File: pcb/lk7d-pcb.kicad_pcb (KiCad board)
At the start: 2 copper layers, 57.2 x 57.2 mm, 32 parts, among them J1 PINHD_1x4_Male, J2 PINHD_1x4_Male, M1 JLCPCB_2DBarcode_5x5mm, SW1 RotaryEncoder_Switch_MP, SW2 RotaryEncoder_Switch_MP, SW3 SW_Push, SW4 SW_Push, SW5 SW_Push, SW6 SW_Push, SW7 SW_Push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

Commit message: Update silkscreen
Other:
- board text added: "C1 and C2 are shared between encoders, solder both for proper filtering."
- board text added: "Documentation: lambdakb.dev/devices/lk7d/"
- board text added: "Only solder one encoder as both of them are wired to the same pins on the MCU."
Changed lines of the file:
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@@
+		(layer "B.SilkS")
+	)
+	(gr_poly
+		(pts
+			(xy 78.675417 39.784027) (xy 78.631132 39.786197) (xy 78.587707 39.789814) (xy 78.545141 39.794878)
+			(xy 78.503433 39.801388) (xy 78.462585 39.809345) (xy 78.422596 39.818749) (xy 78.383465 39.8296)
+			(xy 78.345194 39.841897) (xy 78.307782 39.855642) (xy 78.271228 39.870833) (xy 78.235534 39.88747)
+			(xy 78.200699 39.905555) (xy 78.166722 39.925086) (xy 78.133605 39.946064) (xy 78.101347 39.968489)
+			(xy 78.069552 39.99253) (xy 78.038548 40.018357) (xy 78.008336 40.04597) (xy 77.978914 40.075368)
+			(xy 77.950284 40.106553) (xy 77.922445 40.139523) (xy 77.895398 40.174279) (xy 77.869142 40.210821)
+			(xy 77.843676 40.249149) (xy 77.819002 40.289263) (xy 77.79512 40.331162) (xy 77.772028 40.374848)
+			(xy 77.749728 40.420319) (xy 77.728219 40.467576) (xy 77.707501 40.516619) (xy 77.687574 40.567448)
+			(xy 76.663268 43.255528) (xy 76.648281 43.293664) (xy 76.632976 43.329946) (xy 76.617356 43.364374)
+			(xy 76.601418 43.396949) (xy 76.585165 43.42767) (xy 76.568595 43.456538) (xy 76.551708 43.483551)
+			(xy 76.534505 43.508711) (xy 76.516986 43.532018) (xy 76.49915 43.55347) (xy 76.480997 43.573069)
+			(xy 76.462529 43.590815) (xy 76.443744 43.606707) (xy 76.424642 43.620745) (xy 76.405224 43.632929)
+			(xy 76.38549 43.64326) (xy 76.365314 43.652178) (xy 76.344573 43.660124) (xy 76.323267 43.667098)
+			(xy 76.301396 43.673099) (xy 76.27896 43.678129) (xy 76.255959 43.682187) (xy 76.232393 43.685273)
+			(xy 76.208261 43.687386) (xy 76.183564 43.688528) (xy 76.158303 43.688697) (xy 76.132476 43.687895)
+			(xy 76.106084 43.68612) (xy 76.079127 43.683374) (xy 76.051604 43.679655) (xy 76.023517 43.674964)
+			(xy 75.994864 43.669301) (xy 75.92542 43.651941) (xy 75.769169 44.164093) (xy 75.785988 44.170559)
+			(xy 75.804614 44.176934) (xy 75.82505 44.183218) (xy 75.847294 44.189412) (xy 75.871346 44.195515)
+			(xy 75.897207 44.201528) (xy 75.924877 44.207451) (xy 75.954355 44.213283) (xy 75.985054 44.218709)
+			(xy 76.016385 44.223411) (xy 76.04835 44.22739) (xy 76.080947 44.230645) (xy 76.114177 44.233177)
+			(xy 76.14804 44.234985) (xy 76.182537 44.23607) (xy 76.217666 44.236432) (xy 76.261408 44.235709)
+			(xy 76.304381 44.233538) (xy 76.346585 44.229922) (xy 76.388022 44.224858) (xy 76.428689 44.218347)
+			(xy 76.468588 44.21039) (xy 76.507719 44.200986) (xy 76.54608 44.190136) (xy 76.583674 44.177838)
+			(xy 76.620499 44.164094) (xy 76.656555 44.148903) (xy 76.691842 44.132265) (xy 76.726361 44.114181)
+			(xy 76.760112 44.094649) (xy 76.793093 44.073671) (xy 76.825306 44.051246) (xy 76.856378 44.027194)
+			(xy 76.886658 44.001333) (xy 76.916147 43.973664) (xy 76.944844 43.944186) (xy 76.972751 43.9129)
+			(xy 76.999866 43.879805) (xy 77.02619 43.844902) (xy 77.051723 43.808191) (xy 77.076465 43.769671)
+			(xy 77.100416 43.729342) (xy 77.123575 43.687205) (xy 77.145943 43.64326) (xy 77.16752 43.597506)
+			(xy 77.188306 43.549944) (xy 77.208301 43.500573) (xy 77.227504 43.449394) (xy 77.641277 42.326708)
+			(xy 77.679254 42.218744) (xy 77.715061 42.111864) (xy 77.748698 42.00607) (xy 77.780165 41.901361)
+			(xy 77.810186 41.797194) (xy 77.839483 41.693027) (xy 77.868056 41.58886) (xy 77.895907 41.484694)
+			(xy 77.948713 41.693751) (xy 78.002966 41.904254) (xy 78.016349 41.956428) (xy 78.030455 42.008783)
+			(xy 78.045284 42.061318) (xy 78.060837 42.114034) (xy 78.077113 42.166932) (xy 78.094112 42.22001)
+			(xy 78.111835 42.273268) (xy 78.130281 42.326708) (xy 78.769749 44.164093) (xy 79.458408 44.164093)
+			(xy 78.222874 40.90599) (xy 78.277851 40.752633) (xy 78.291776 40.71452) (xy 78.306063 40.678306)
+			(xy 78.320711 40.64399) (xy 78.335721 40.611574) (xy 78.351093 40.581056) (xy 78.366827 40.552438)
+			(xy 78.382922 40.525718) (xy 78.399379 40.500897) (xy 78.416197 40.477975) (xy 78.433378 40.456951)
+			(xy 78.45092 40.437827) (xy 78.468823 40.420601) (xy 78.487089 40.405275) (xy 78.505716 40.391847)
+			(xy 78.524705 40.380318) (xy 78.544055 40.370688) (xy 78.563959 40.362505) (xy 78.584609 40.355316)
+			(xy 78.606006 40.349123) (xy 78.628148 40.343923) (xy 78.651036 40.339719) (xy 78.67467 40.336509)
+			(xy 78.69905 40.334293) (xy 78.724177 40.333073) (xy 78.750049 40.332847) (xy 78.776667 40.333615)
+			(xy 78.804031 40.335378) (xy 78.832141 40.338136) (xy 78.860997 40.341889) (xy 78.890599 40.346636)
+			(xy 78.920947 40.352378) (xy 78.952041 40.359114) (xy 79.015699 40.370688) (xy 79.17195 39.852748)
+			(xy 79.163755 39.849165) (xy 79.155086 39.84565) (xy 79.145942 39.842203) (xy 79.136323 39.838823)
+			(xy 79.115662 39.832267) (xy 79.093101 39.825983) (xy 79.068642 39.81997) (xy 79.042284 39.814228)
+			(xy 79.014027 39.808757) (xy 78.983871 39.803558) (xy 78.951907 39.798811) (xy 78.919671 39.794697)
+			(xy 78.887164 39.791216) (xy 78.854386 39.788367) (xy 78.821336 39.786152) (xy 78.788015 39.78457)
+			(xy 78.754423 39.78362) (xy 78.72056 39.783304)
+		)
+		(stroke
+			(width -0.000001)
+			(type solid)
+		)
+		(fill yes)
 		(layer "B.SilkS")
 	)
@@
 		(layer "Dwgs.User")
 	)
+	(gr_poly
+		(pts
+			(xy 75.134337 44.489318) (xy 80.114361 44.489318) (xy 80.114361 39.509294) (xy 75.134337 39.509294)
+		)
+		(stroke
+			(width 0.119973)
+			(type solid)
+		)
+		(fill no)
+		(layer "Dwgs.User")
+	)
 	(gr_arc
 		(start 87.15 85.15)
@@
 		)
 		(layer "Edge.Cuts")
+	)
+	(gr_text "C1 and C2 are shared\nbetween encoders, solder\nboth for proper filtering."
+		(at 41.5 50.75 0)
+		(layer "B.SilkS")
+		(effects
+			(font
+				(size 0.6 0.6)
+				(thickness 0.12)
+			)
+			(justify bottom mirror)
+		)
 	)
 	(gr_text "CERN-OHL-S-2.0"
@@
 		)
 	)
+	(gr_text "Documentation:\nlambdakb.dev/devices/lk7d/"
+		(at 30.75 73.25 270)
+		(layer "B.SilkS")
+		(effects
+			(font
+				(size 0.7 0.7)
+				(thickness 0.12)
+				(bold yes)
+			)
+			(justify left bottom mirror)
+		)
+	)
 	(gr_text "Licensed under"
 		(at 64.6 68.275 0)
@@
 			)
 			(justify left bottom mirror)
+		)
+	)
+	(gr_text "Only solder one encoder as\nboth of them are wired to\nthe same pins on the MCU."
+		(at 75.65 50.75 0)
+		(layer "B.SilkS")
+		(effects
+			(font
+				(size 0.6 0.6)
+				(thickness 0.12)
+			)
+			(justify bottom mirror)
 		)
 	)
@@
 	)
 	(group ""
+		(members "b9afdcb9-ae57-4a90-9416-50e6e42f6fef" "d71c0996-1f6c-4e7b-8f96-d0375cd077d0")
+	)
+	(group ""

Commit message: Fix Data Matrix Code positioning following JLCPCB feedbacks
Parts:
- moved M1 0.50 mm to (39.5, 42.5)

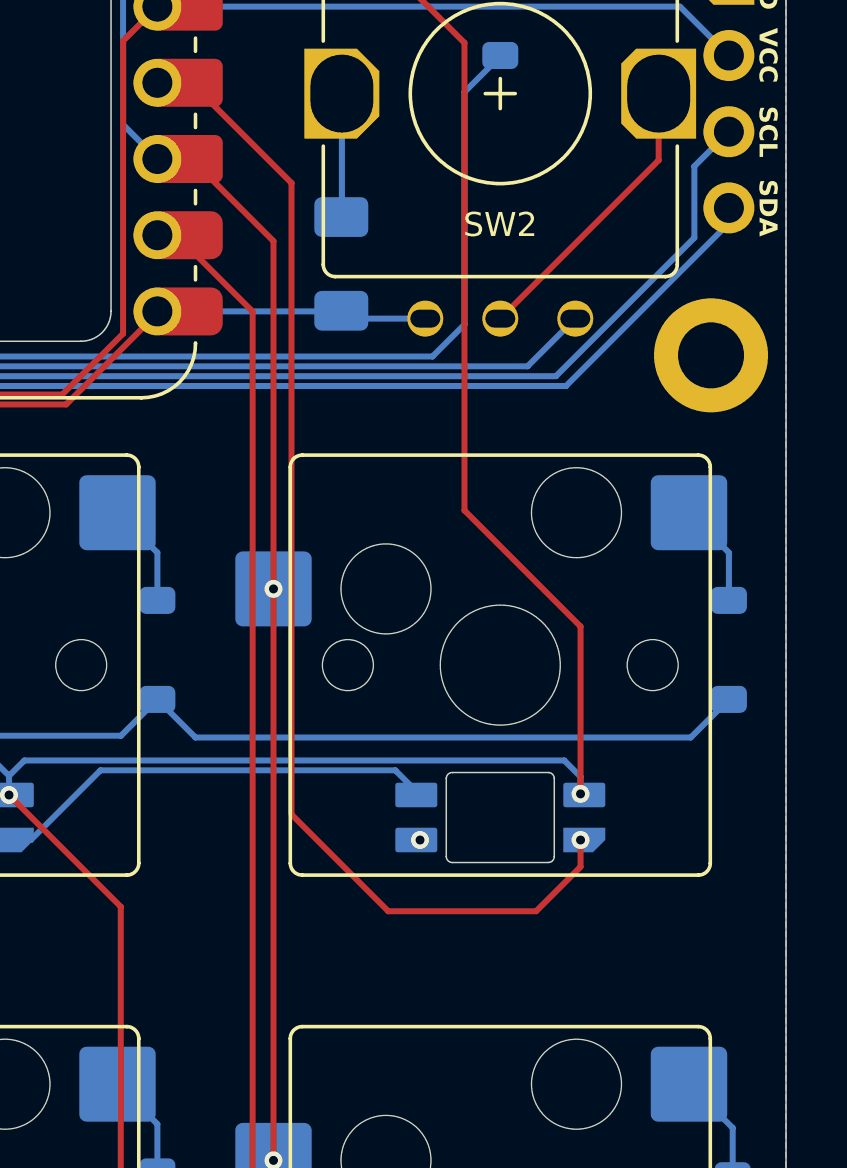
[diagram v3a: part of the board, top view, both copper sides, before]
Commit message: Add Logic Level Converter for per keys LEDs
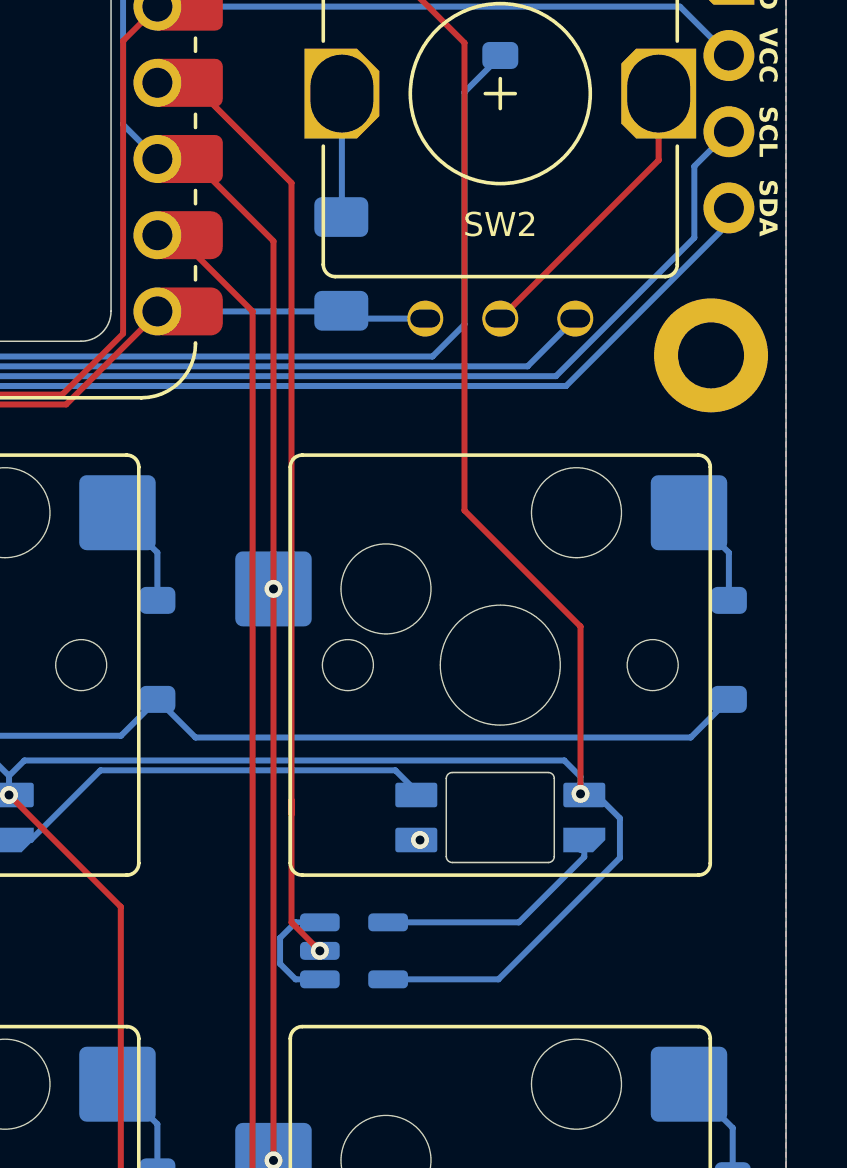
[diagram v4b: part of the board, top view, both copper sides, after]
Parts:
- added U2: SN74LV1T125DBV, Package_TO_SOT_SMD:SOT-23-5, B.Cu at (72.7, 68.1)
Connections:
- U1 pad 11: /LED -> /LEDIO
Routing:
- net /LEDIO: track 0.00 -> 32.3 mm, vias 0 -> 1
- net /LED: track 39.4 -> 8.34 mm, vias 1 -> 0
- net +5V: track 145.3 -> 157.5 mm
- net GND: track 41.5 -> 45.4 mm

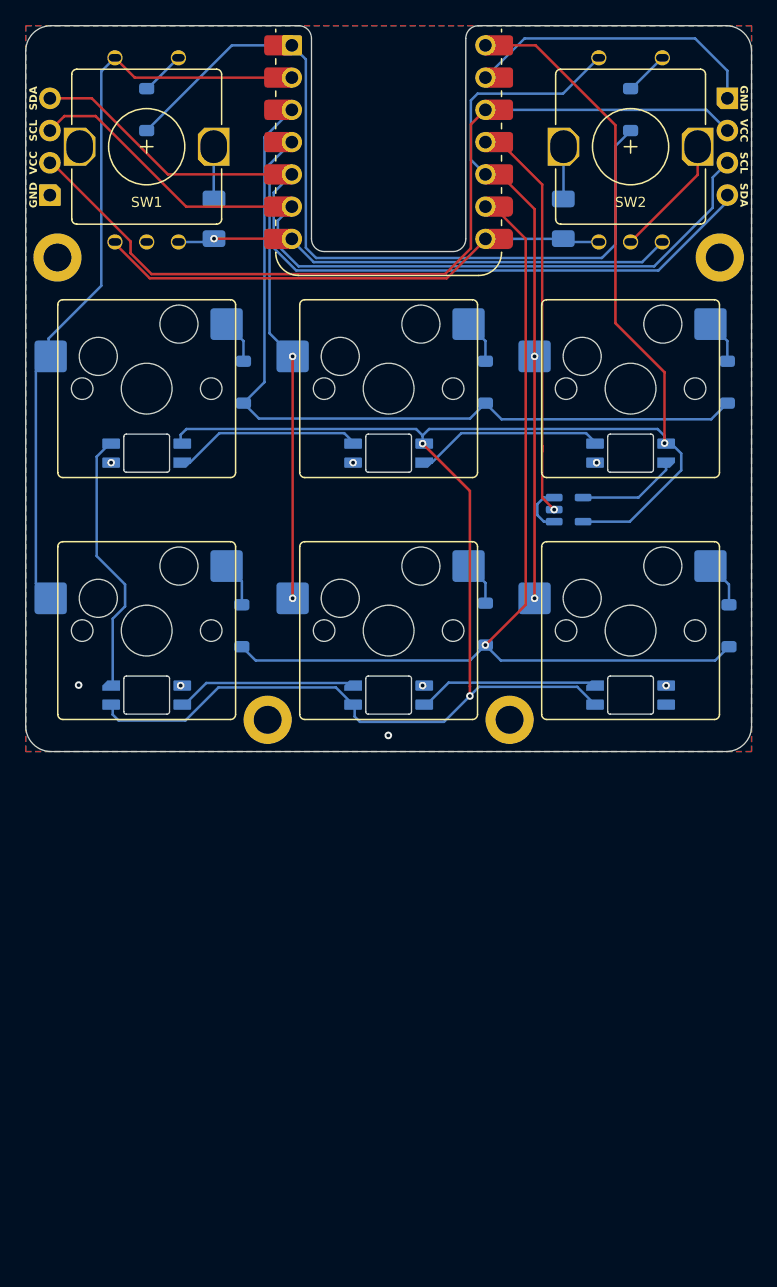
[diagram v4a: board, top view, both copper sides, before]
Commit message: Fix SK6812MINI-E pin mapping
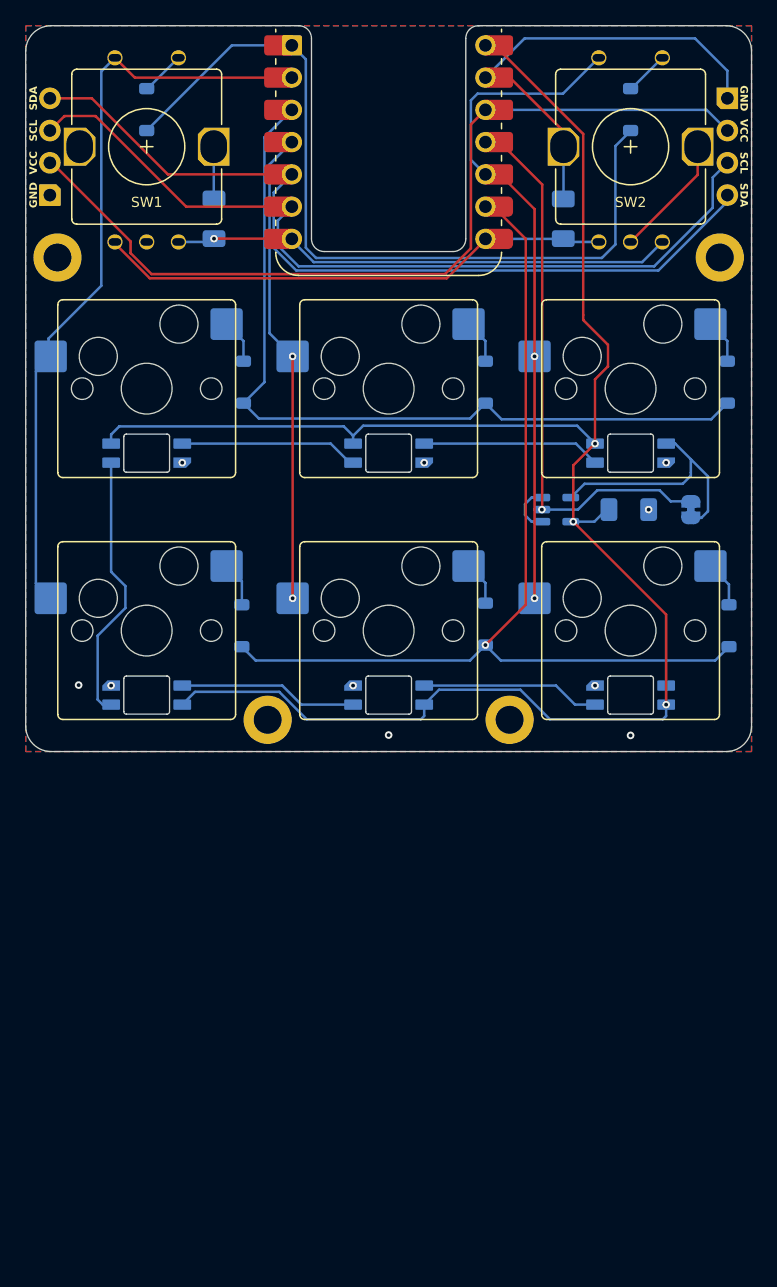
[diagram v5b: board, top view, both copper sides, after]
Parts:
- added C3: 100nF, Capacitor_SMD:C_1206_3216Metric_Pad1.33x1.80mm_HandSolder, B.Cu at (77.5, 68.1)
- added JP1: SolderJumper_2_Bridged, Jumper:SolderJumper-2_P1.3mm_Bridged_RoundedPad1.0x1.5mm, B.Cu at (82.4, 68.1)
- moved U2 0.97 mm to (71.8, 68.1)
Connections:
- LED1 pad 1: Net-(LED1-DOUT) -> +5V
- LED1 pad 2: GND -> Net-(LED1-DOUT)
- LED1 pad 3: /LED -> GND
- LED1 pad 4: +5V -> /LEDIN
- LED2 pad 1: Net-(LED2-DOUT) -> +5V
- LED2 pad 2: GND -> Net-(LED2-DOUT)
- LED2 pad 3: Net-(LED1-DOUT) -> GND
- LED2 pad 4: +5V -> Net-(LED1-DOUT)
- LED3 pad 1: Net-(LED3-DOUT) -> +5V
- LED3 pad 2: GND -> Net-(LED3-DOUT)
- LED3 pad 3: Net-(LED2-DOUT) -> GND
- LED3 pad 4: +5V -> Net-(LED2-DOUT)
- LED4 pad 1: Net-(LED4-DOUT) -> +5V
- LED4 pad 2: GND -> Net-(LED4-DOUT)
- LED4 pad 3: Net-(LED3-DOUT) -> GND
- LED4 pad 4: +5V -> Net-(LED3-DOUT)
- LED5 pad 1: Net-(LED5-DOUT) -> +5V
- LED5 pad 2: GND -> Net-(LED5-DOUT)
- LED5 pad 3: Net-(LED4-DOUT) -> GND
- LED5 pad 4: +5V -> Net-(LED4-DOUT)
- LED6 pad 1: unconnected-(LED6-DOUT-Pad1) -> +5V
- LED6 pad 2: GND -> unconnected-(LED6-DOUT-Pad2)
- LED6 pad 3: Net-(LED5-DOUT) -> GND
- LED6 pad 4: +5V -> Net-(LED5-DOUT)
- U2 pad 4: /LED -> /LEDIN
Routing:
- net /LEDIN: track 0.00 -> 20.8 mm
- net /LEDIO: track 32.3 -> 44.4 mm
- net +5V: track 157.5 -> 147.0 mm
- net GND: track 45.4 -> 54.0 mm, vias 8 -> 10
- net /LED: track 8.34 -> 0.00 mm
- net Net-(LED2-DOUT): track 15.0 -> 14.1 mm
- net Net-(LED1-DOUT): track 15.0 -> 14.1 mm
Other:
- board text added: "LEDs run on 3.3V logic by default. If your LEDS require 5V logic, cut JP1 and populate U2 and C3."
- board text added: "LK7D v1.01"
- board text removed: "LK7D v1.00"

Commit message: Add plate and cleanup PCB (#4)
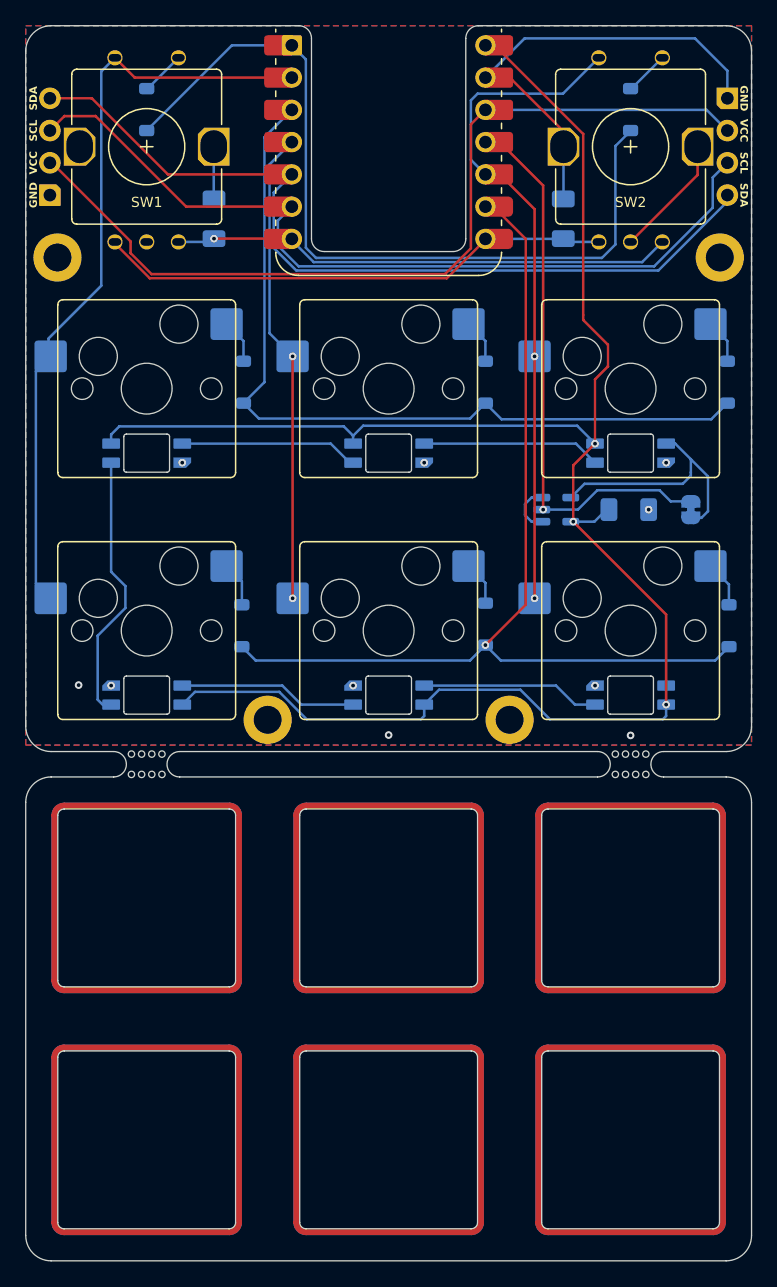
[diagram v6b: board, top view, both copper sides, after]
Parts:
- added CUT1: Plate_MX_1U, LKBD_PlateMX:Plate_MX_1U, F.Cu at (39.5, 98.7)
- added CUT2: Plate_MX_1U, LKBD_PlateMX:Plate_MX_1U, F.Cu at (58.6, 98.7)
- added CUT3: Plate_MX_1U, LKBD_PlateMX:Plate_MX_1U, F.Cu at (77.6, 98.7)
- added CUT4: Plate_MX_1U, LKBD_PlateMX:Plate_MX_1U, F.Cu at (39.5, 117.7)
- added CUT5: Plate_MX_1U, LKBD_PlateMX:Plate_MX_1U, F.Cu at (58.6, 117.7)
- added CUT6: Plate_MX_1U, LKBD_PlateMX:Plate_MX_1U, F.Cu at (77.6, 117.7)
- added MB1: MouseBite_2.0x3.2mm, LKBD_Common:MouseBite_2.0x3.2mm, F.Cu at (39.5, 88.2)
- added MB2: MouseBite_2.0x3.2mm, LKBD_Common:MouseBite_2.0x3.2mm, F.Cu at (77.6, 88.2)
- C1, C2, C3: footprint Capacitor_SMD:C_1206_3216Metric_Pad1.33x1.80mm_HandSolder -> LKBD_Common:Capacitor_SMD_1206_inSilk
- D1, D2, D3, D4, D5, D6, D7, D8: footprint Diode_SMD:D_SOD-123 -> LKBD_Common:Diode_SMD_SOD-123_inSilk
- turned SW3 to 180 degrees
- turned SW4 to 180 degrees
- turned SW5 to 180 degrees
- turned SW6 to 180 degrees
- turned SW7 to 180 degrees
- turned SW8 to 180 degrees
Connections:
- SW1 pad S1: Net-(D1-A) -> /COL0
- SW1 pad S2: /COL0 -> Net-(D1-A)
- SW2 pad S1: Net-(D2-A) -> /COL2
- SW2 pad S2: /COL2 -> Net-(D2-A)
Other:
- board size 57.2 x 57.2 mm -> 57.2 x 97.2 mm

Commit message: Make plate a separate PCB (#6)
* Make the plate a separate PCB

* Update PCB 3D models and add layout to README.md

* Format README.md
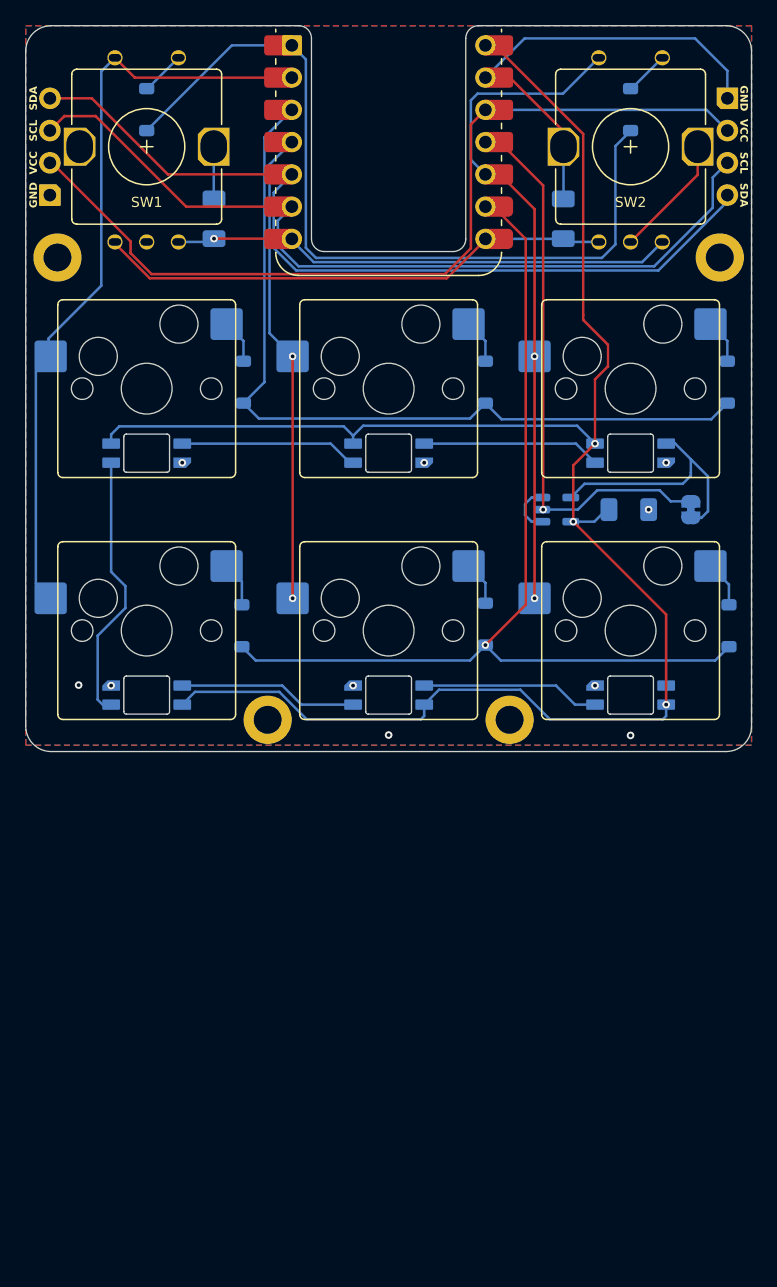
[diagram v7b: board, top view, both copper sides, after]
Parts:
- removed CUT1, CUT2, CUT3, CUT4, CUT5, CUT6: Plate_MX_1U, LKBD_PlateMX:Plate_MX_1U
- removed MB1, MB2: MouseBite_2.0x3.2mm, LKBD_Common:MouseBite_2.0x3.2mm
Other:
- board size 57.2 x 97.2 mm -> 57.2 x 57.2 mm
